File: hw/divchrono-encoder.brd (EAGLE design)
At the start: 100 x 80 mm, 8 parts, among them U1 PIC16F54-I/P, X1 32KHz

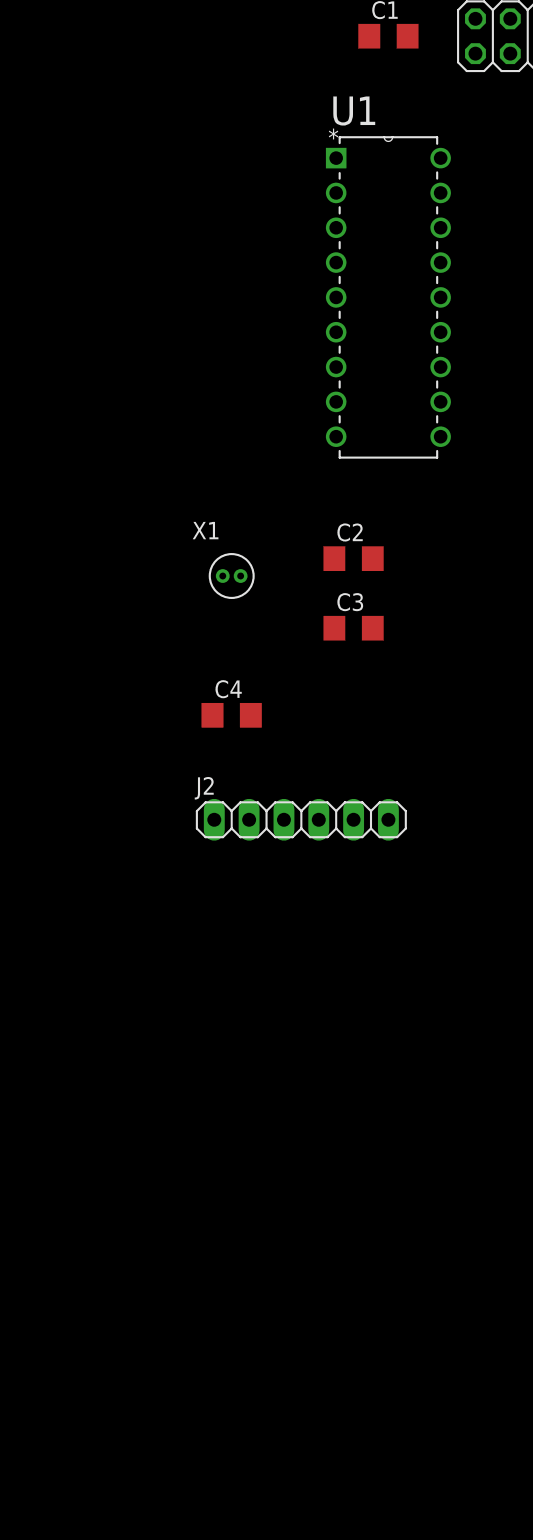
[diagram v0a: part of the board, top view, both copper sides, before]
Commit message: Updated encoder board and documentation for new design using a SN74HC148 encoder instead of a custom PIC.
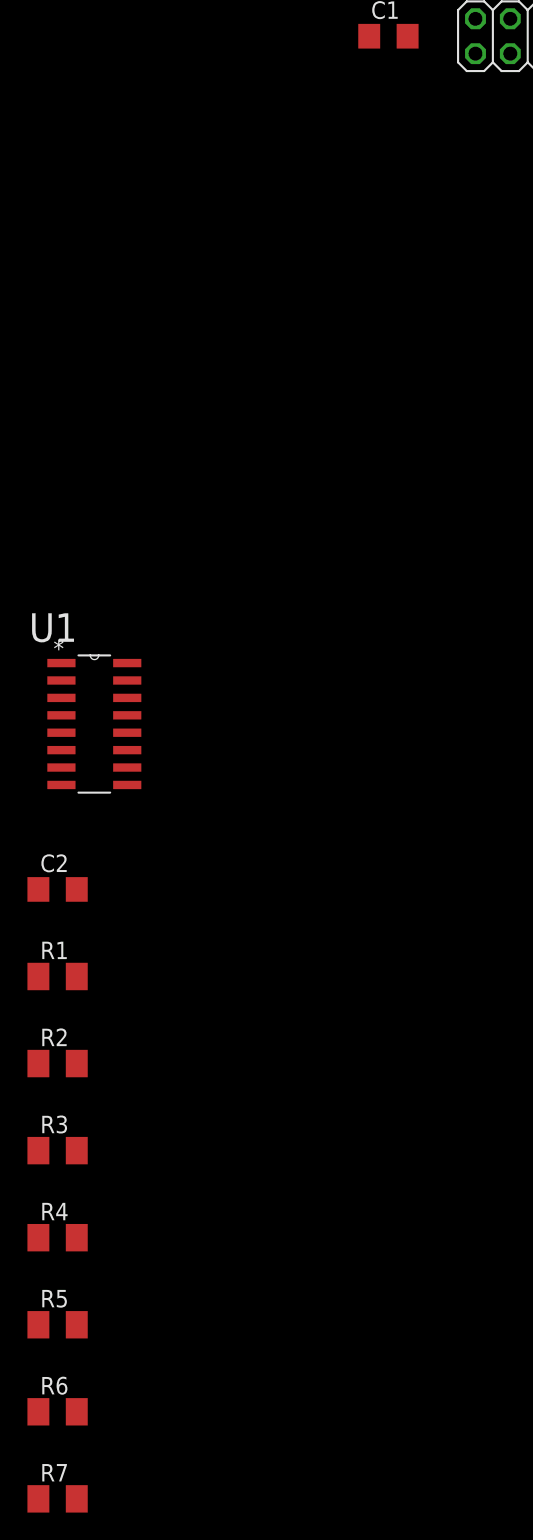
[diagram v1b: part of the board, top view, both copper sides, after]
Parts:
- removed C3: 22pF, rcl:C1206
- removed C4: 100nF, rcl:C1206
- removed J2: (no value), pinhead:1X06
- removed X1: 32KHz, pgrmcount:WATCH-3X8
- added R1, R2, R3, R4, R5, R6, R7: 1M, rcl:M1206
- C2: value 22pF -> 100nF
- U1: value PIC16F54-I/P -> SN74HC148D; device Microchip_By_element14_Batch_1:DIP254P762X533-18 -> Texas Instruments_By_element14_Batch_1:SOIC127P600X175-16N
- moved U1 34.2 mm to (-45.7, -20.3)
- moved C2 32.4 mm to (-50.8, -27.9)
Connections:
- removed net OSC1: C2.1, U1.16, X1.1
- removed net OSC2: C3.1, U1.15, X1.2
- removed net PGC: J2.5, U1.12
- removed net PGD: J2.4, U1.13
- removed net VPP: J2.1, U1.4
- net +3V3: now also C2.1, R1.2, R2.2, R3.2, R4.2, R5.2, R6.2, R7.2, U1.10, U1.16; no longer C4.1, J2.2, U1.14
- net 1: now also R1.1, U1.11; no longer U1.17
- net 2: now also R2.1, U1.12; no longer U1.18
- net 3: now also R3.1
- net 4: now also R4.1, U1.13; no longer U1.2
- net 5: now also R5.1, U1.2; no longer U1.9
- net 6: now also R6.1, U1.3; no longer U1.10
- net 7: now also R7.1, U1.4; no longer U1.11
- net D1: now also U1.9; no longer U1.6
- net D3: now also U1.6; no longer U1.8
- net GND: now also U1.8; no longer C3.2, C4.2, J2.3
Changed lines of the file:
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@@
 <element name="C1" library="rcl" package="C1206" value="100nF" x="-26.67" y="34.29"/>
 <element name="J1" library="pinhead" package="2X03" value="" x="-17.78" y="34.29"/>
-<element name="U1" library="Microchip_By_element14_Batch_1" package="DIP254P762X533-18" value="PIC16F54-I/P" x="-22.86" y="5.08">
-<attribute name="OC_FARNELL" value="1212691" x="-22.86" y="5.08" size="1.778" layer="27" display="off"/>
-<attribute name="SUPPLIER" value="Microchip" x="-22.86" y="5.08" size="1.778" layer="27" display="off"/>
-<attribute name="PACKAGE" value="DIP-18" x="-22.86" y="5.08" size="1.778" layer="27" display="off"/>
-<attribute name="MPN" value="PIC16F54-I/P" x="-22.86" y="5.08" size="1.778" layer="27" display="off"/>
-<attribute name="OC_NEWARK" value="89H0459" x="-22.86" y="5.08" size="1.778" layer="27" display="off"/>
+<element name="U1" library="Texas Instruments_By_element14_Batch_1" package="SOIC127P600X175-16N" value="SN74HC148D" x="-45.72" y="-20.32">
+<attribute name="PACKAGE" value="SOIC-16" x="-45.72" y="-20.32" size="1.778" layer="27" display="off"/>
+<attribute name="OC_FARNELL" value="1287478" x="-45.72" y="-20.32" size="1.778" layer="27" display="off"/>
+<attribute name="SUPPLIER" value="Texas Instruments" x="-45.72" y="-20.32" size="1.778" layer="27" display="off"/>
+<attribute name="MPN" value="SN74HC148D" x="-45.72" y="-20.32" size="1.778" layer="27" display="off"/>
+<attribute name="OC_NEWARK" value="35K0804" x="-45.72" y="-20.32" size="1.778" layer="27" display="off"/>
 </element>
-<element name="C2" library="rcl" package="C1206" value="22pF" x="-29.21" y="-3.81"/>
-<element name="C3" library="rcl" package="C1206" value="22pF" x="-29.21" y="-8.89"/>
-<element name="X1" library="pgrmcount" package="WATCH-3X8" value="32KHz" x="-38.1" y="-5.08"/>
-<element name="C4" library="rcl" package="C1206" value="100nF" x="-38.1" y="-15.24"/>
-<element name="J2" library="pinhead" package="1X06" value="" x="-33.02" y="-22.86"/>
+<element name="C2" library="rcl" package="C1206" value="100nF" x="-50.8" y="-27.94"/>
+<element name="R1" library="rcl" package="M1206" value="1M" x="-50.8" y="-34.29"/>
+<element name="R2" library="rcl" package="M1206" value="1M" x="-50.8" y="-40.64"/>
+<element name="R3" library="rcl" package="M1206" value="1M" x="-50.8" y="-46.99"/>
+<element name="R4" library="rcl" package="M1206" value="1M" x="-50.8" y="-53.34"/>
+<element name="R5" library="rcl" package="M1206" value="1M" x="-50.8" y="-59.69"/>
+<element name="R6" library="rcl" package="M1206" value="1M" x="-50.8" y="-66.04"/>
+<element name="R7" library="rcl" package="M1206" value="1M" x="-50.8" y="-72.39"/>
 </elements>
 <signals>
 <signal name="D1">
 <contactref element="J1" pad="1"/>
-<contactref element="U1" pad="6"/>
-<wire x1="-20.32" y1="33.02" x2="-30.48" y2="12.7" width="0" layer="19" extent="1-1"/>
+<contactref element="U1" pad="9"/>
+<wire x1="-20.32" y1="33.02" x2="-45.72" y2="-20.32" width="0" layer="19" extent="1-1"/>
 </signal>
 <signal name="D2">
 <contactref element="J1" pad="3"/>
 <contactref element="U1" pad="7"/>
-<wire x1="-17.78" y1="33.02" x2="-30.48" y2="10.16" width="0" layer="19" extent="1-1"/>
+<wire x1="-17.78" y1="33.02" x2="-50.5206" y2="-19.05" width="0" layer="19" extent="1-1"/>
 </signal>
 <signal name="D3">
 <contactref element="J1" pad="5"/>
-<contactref element="U1" pad="8"/>
-<wire x1="-15.24" y1="33.02" x2="-30.48" y2="7.62" width="0" layer="19" extent="1-1"/>
+<contactref element="U1" pad="6"/>
+<wire x1="-15.24" y1="33.02" x2="-50.5206" y2="-17.78" width="0" layer="19" extent="1-1"/>
 </signal>
 <signal name="+3V3">
 <contactref element="J1" pad="2"/>
 <contactref element="C1" pad="1"/>
-<contactref element="U1" pad="14"/>
-<contactref element="C4" pad="1"/>
-<contactref element="J2" pad="2"/>
-<wire x1="-39.5" y1="-15.24" x2="-36.83" y2="-22.86" width="0" layer="19" extent="1-1"/>
-<wire x1="-22.86" y1="15.24" x2="-39.5" y2="-15.24" width="0" layer="19" extent="1-1"/>
-<wire x1="-28.07" y1="34.29" x2="-22.86" y2="15.24" width="0" layer="19" extent="1-1"/>
+<contactref element="U1" pad="10"/>
+<contactref element="U1" pad="16"/>
+<contactref element="C2" pad="1"/>
+<contactref element="R7" pad="2"/>
+<contactref element="R6" pad="2"/>
+<contactref element="R5" pad="2"/>
+<contactref element="R4" pad="2"/>
+<contactref element="R3" pad="2"/>
+<contactref element="R2" pad="2"/>
+<contactref element="R1" pad="2"/>
+<wire x1="-49.4" y1="-66.04" x2="-49.4" y2="-72.39" width="0" layer="19" extent="1-1"/>
+<wire x1="-49.4" y1="-59.69" x2="-49.4" y2="-66.04" width="0" layer="19" extent="1-1"/>
+<wire x1="-49.4" y1="-53.34" x2="-49.4" y2="-59.69" width="0" layer="19" extent="1-1"/>
+<wire x1="-49.4" y1="-46.99" x2="-49.4" y2="-53.34" width="0" layer="19" extent="1-1"/>
+<wire x1="-49.4" y1="-40.64" x2="-49.4" y2="-46.99" width="0" layer="19" extent="1-1"/>
+<wire x1="-49.4" y1="-34.29" x2="-49.4" y2="-40.64" width="0" layer="19" extent="1-1"/>
+<wire x1="-52.2" y1="-27.94" x2="-49.4" y2="-34.29" width="0" layer="19" extent="1-1"/>
+<wire x1="-45.72" y1="-19.05" x2="-52.2" y2="-27.94" width="0" layer="19" extent="1-1"/>
+<wire x1="-45.72" y1="-11.43" x2="-45.72" y2="-19.05" width="0" layer="19" extent="1-1"/>
+<wire x1="-28.07" y1="34.29" x2="-45.72" y2="-11.43" width="0" layer="19" extent="1-1"/>
 <wire x1="-20.32" y1="35.56" x2="-28.07" y2="34.29" width="0" layer="19" extent="1-1"/>
 </signal>
@@
 <contactref element="C1" pad="2"/>
 <contactref element="U1" pad="5"/>
-<contactref element="C3" pad="2"/>
+<contactref element="U1" pad="8"/>
 <contactref element="C2" pad="2"/>
-<contactref element="C4" pad="2"/>
-<contactref element="J2" pad="3"/>
-<wire x1="-36.7" y1="-15.24" x2="-34.29" y2="-22.86" width="0" layer="19" extent="1-1"/>
-<wire x1="-27.81" y1="-8.89" x2="-36.7" y2="-15.24" width="0" layer="19" extent="1-1"/>
-<wire x1="-27.81" y1="-3.81" x2="-27.81" y2="-8.89" width="0" layer="19" extent="1-1"/>
-<wire x1="-30.48" y1="15.24" x2="-27.81" y2="-3.81" width="0" layer="19" extent="1-1"/>
-<wire x1="-25.27" y1="34.29" x2="-30.48" y2="15.24" width="0" layer="19" extent="1-1"/>
+<wire x1="-50.5206" y1="-20.32" x2="-49.4" y2="-27.94" width="0" layer="19" extent="1-1"/>
+<wire x1="-50.5206" y1="-16.51" x2="-50.5206" y2="-20.32" width="0" layer="19" extent="1-1"/>
+<wire x1="-25.27" y1="34.29" x2="-50.5206" y2="-16.51" width="0" layer="19" extent="1-1"/>
 <wire x1="-15.24" y1="35.56" x2="-25.27" y2="34.29" width="0" layer="19" extent="1-1"/>
 </signal>
-<signal name="OSC1">
-<contactref element="U1" pad="16"/>
-<contactref element="X1" pad="1"/>
-<contactref element="C2" pad="1"/>
-<wire x1="-30.61" y1="-3.81" x2="-38.7516" y2="-5.08" width="0" layer="19" extent="1-1"/>
-<wire x1="-22.86" y1="20.32" x2="-30.61" y2="-3.81" width="0" layer="19" extent="1-1"/>
-</signal>
-<signal name="OSC2">
-<contactref element="U1" pad="15"/>
-<contactref element="X1" pad="2"/>
-<contactref element="C3" pad="1"/>
-<wire x1="-30.61" y1="-8.89" x2="-37.4484" y2="-5.08" width="0" layer="19" extent="1-1"/>
-<wire x1="-22.86" y1="17.78" x2="-37.4484" y2="-5.08" width="0" layer="19" extent="1-1"/>
-</signal>
-<signal name="VPP">
-<contactref element="U1" pad="4"/>
-<contactref element="J2" pad="1"/>
-<wire x1="-30.48" y1="17.78" x2="-39.37" y2="-22.86" width="0" layer="19" extent="1-1"/>
-</signal>
 <signal name="1">
-<contactref element="U1" pad="17"/>
+<contactref element="U1" pad="11"/>
+<contactref element="R1" pad="1"/>
+<wire x1="-45.72" y1="-17.78" x2="-52.2" y2="-34.29" width="0" layer="19" extent="1-1"/>
 </signal>
 <signal name="2">
-<contactref element="U1" pad="18"/>
+<contactref element="U1" pad="12"/>
+<contactref element="R2" pad="1"/>
+<wire x1="-45.72" y1="-16.51" x2="-52.2" y2="-40.64" width="0" layer="19" extent="1-1"/>
 </signal>
 <signal name="3">
 <contactref element="U1" pad="1"/>
+<contactref element="R3" pad="1"/>
+<wire x1="-50.5206" y1="-11.43" x2="-52.2" y2="-46.99" width="0" layer="19" extent="1-1"/>
 </signal>
 <signal name="4">
-<contactref element="U1" pad="2"/>
+<contactref element="U1" pad="13"/>
+<contactref element="R4" pad="1"/>
+<wire x1="-45.72" y1="-15.24" x2="-52.2" y2="-53.34" width="0" layer="19" extent="1-1"/>
 </signal>
 <signal name="5">
-<contactref element="U1" pad="9"/>
+<contactref element="U1" pad="2"/>
+<contactref element="R5" pad="1"/>
+<wire x1="-50.5206" y1="-12.7" x2="-52.2" y2="-59.69" width="0" layer="19" extent="1-1"/>
 </signal>
 <signal name="6">
-<contactref element="U1" pad="10"/>
+<contactref element="U1" pad="3"/>
+<contactref element="R6" pad="1"/>
+<wire x1="-50.5206" y1="-13.97" x2="-52.2" y2="-66.04" width="0" layer="19" extent="1-1"/>
 </signal>
 <signal name="7">
-<contactref element="U1" pad="11"/>
-</signal>
-<signal name="PGD">
-<contactref element="J2" pad="4"/>
-<contactref element="U1" pad="13"/>
-<wire x1="-22.86" y1="12.7" x2="-31.75" y2="-22.86" width="0" layer="19" extent="1-1"/>
-</signal>
-<signal name="PGC">
-<contactref element="J2" pad="5"/>
-<contactref element="U1" pad="12"/>
-<wire x1="-22.86" y1="10.16" x2="-29.21" y2="-22.86" width="0" layer="19" extent="1-1"/>
+<contactref element="U1" pad="4"/>
+<contactref element="R7" pad="1"/>
+<wire x1="-50.5206" y1="-15.24" x2="-52.2" y2="-72.39" width="0" layer="19" extent="1-1"/>
 </signal>
 </signals>

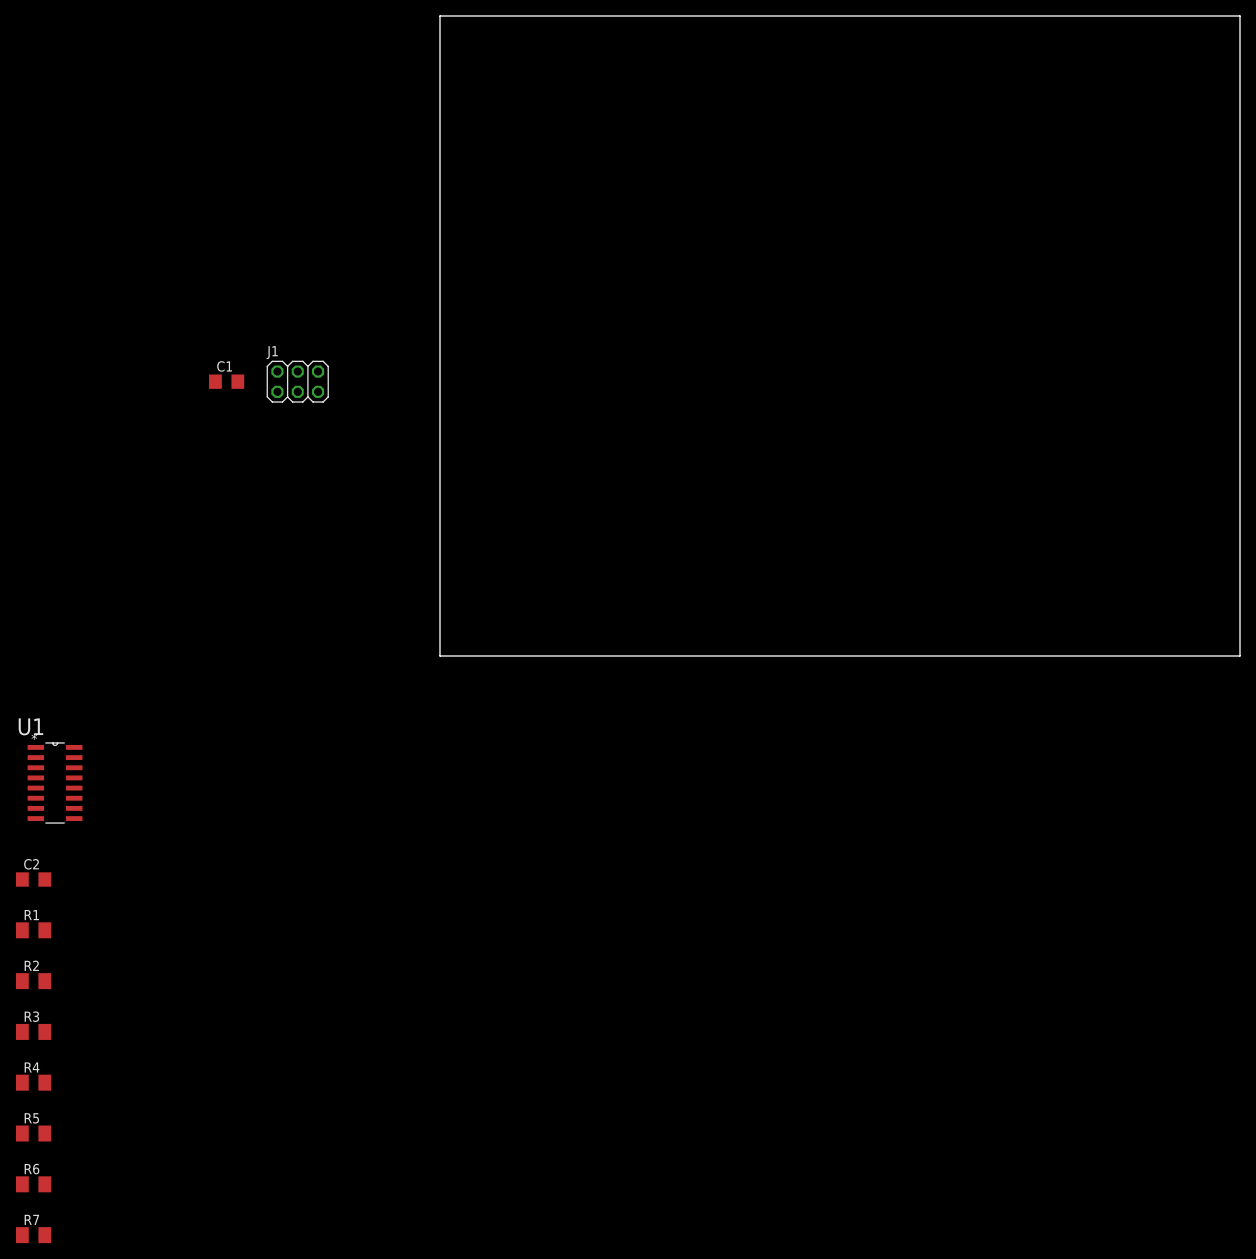
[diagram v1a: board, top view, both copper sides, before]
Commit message: Finished initial encoder board schematic and layout. Checked ERC/DRC, updated documentation, and compiled gerbers.
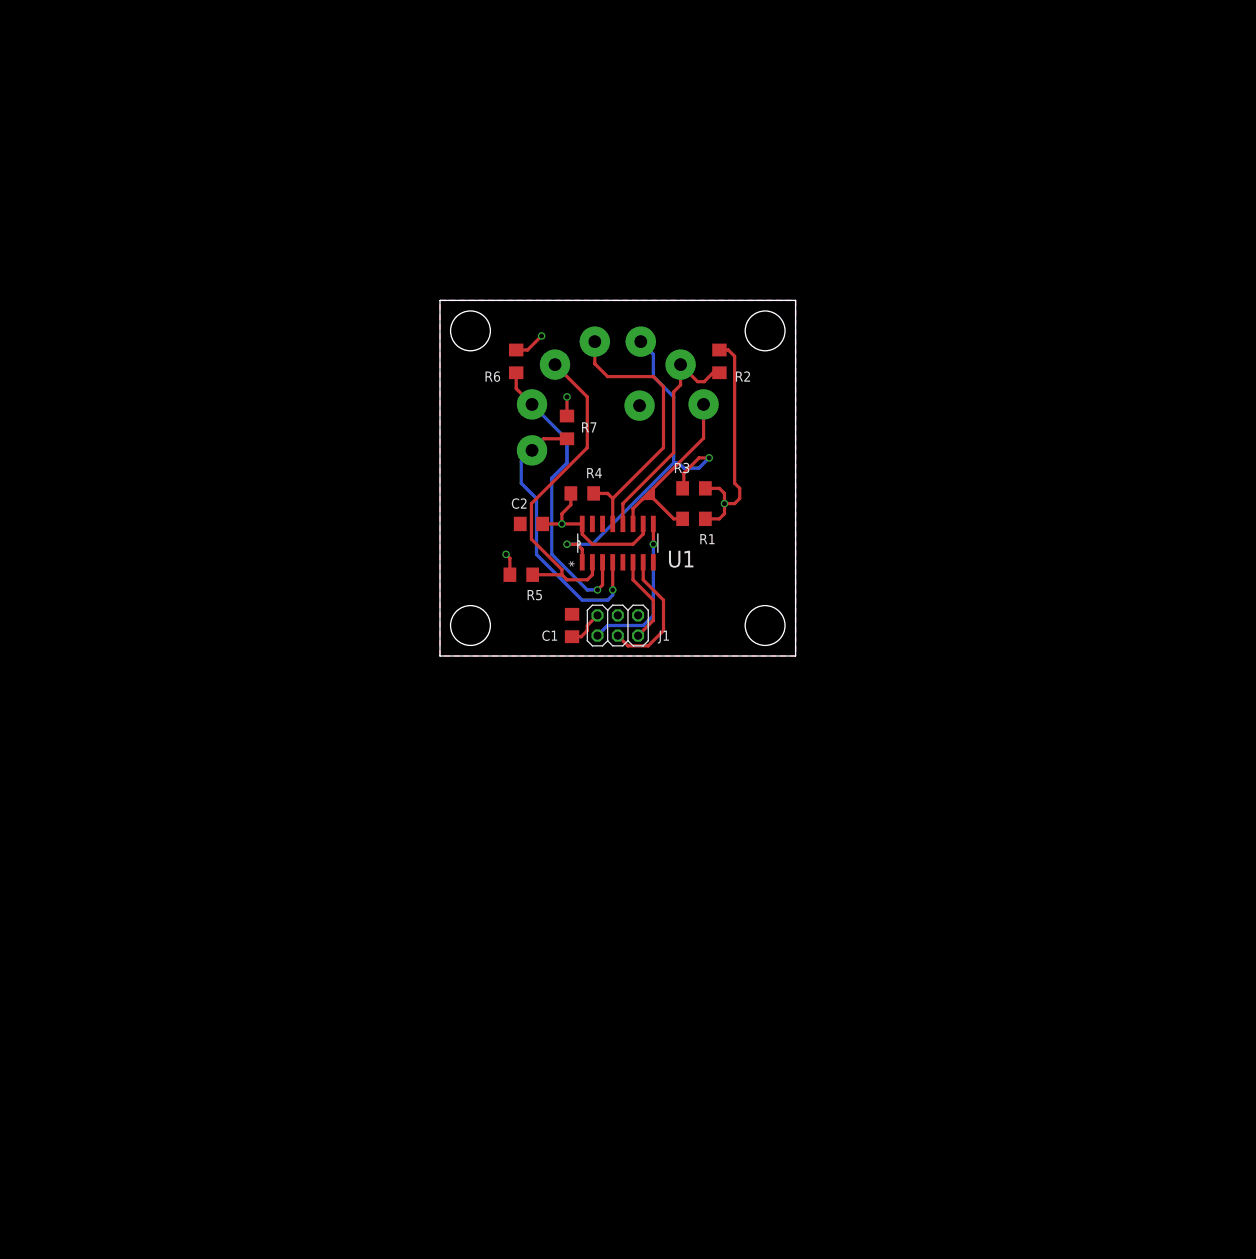
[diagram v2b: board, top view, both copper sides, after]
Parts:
- added S1: CKN10616, divchrono:CKN10616
- R1, R2, R3, R4, R5, R6, R7: device rcl:M1206 -> rcl:R1206
- moved R7 121.0 mm to (15.9, 28.6), turned to 90 degrees
- moved R6 119.3 mm to (9.53, 36.8), turned to 90 degrees
- moved R2 115.5 mm to (34.9, 36.8), turned to 90 degrees
- moved R3 106.9 mm to (31.8, 21.0)
- moved R4 100.6 mm to (17.8, 20.3), turned to 180 degrees
- moved R1 97.3 mm to (31.8, 17.1)
- moved R5 92.7 mm to (10.2, 10.2), turned to 180 degrees
- moved U1 81.2 mm to (26.7, 16.5), turned to 90 degrees
- moved C2 76.5 mm to (11.4, 16.5), turned to 180 degrees
- moved C1 52.9 mm to (16.5, 3.81), turned to 90 degrees
- moved J1 50.3 mm to (22.2, 3.81)
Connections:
- net 1: now also S1.1
- net 2: now also S1.2
- net 3: now also S1.3
- net 4: now also S1.4
- net 5: now also S1.5
- net 6: now also S1.6
- net 7: now also S1.7
- net GND: now also S1.A
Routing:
- net +3V3: track 0.00 -> 64.4 mm, vias 0 -> 5
- net 3: track 0.00 -> 49.4 mm, vias 0 -> 2
- net 5: track 0.00 -> 42.0 mm
- net 6: track 0.00 -> 37.4 mm, vias 0 -> 1
- net 7: track 0.00 -> 35.6 mm, vias 0 -> 1
- net 4: track 0.00 -> 35.0 mm
- net 2: track 0.00 -> 29.1 mm
- net 1: track 0.00 -> 27.5 mm
- net D1: track 0.00 -> 19.5 mm, vias 0 -> 1
- net D2: track 0.00 -> 16.6 mm
- net D3: track 0.00 -> 11.0 mm
- added copper zone on layer 16, net +3V3
- added copper zone on layer 1, net GND
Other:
- board size 100 x 80 mm -> 44.5 x 44.5 mm
